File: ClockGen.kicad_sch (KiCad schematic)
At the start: 26 parts, among them Q1 2N4258, Q2 2N4258, Y1 XT0001

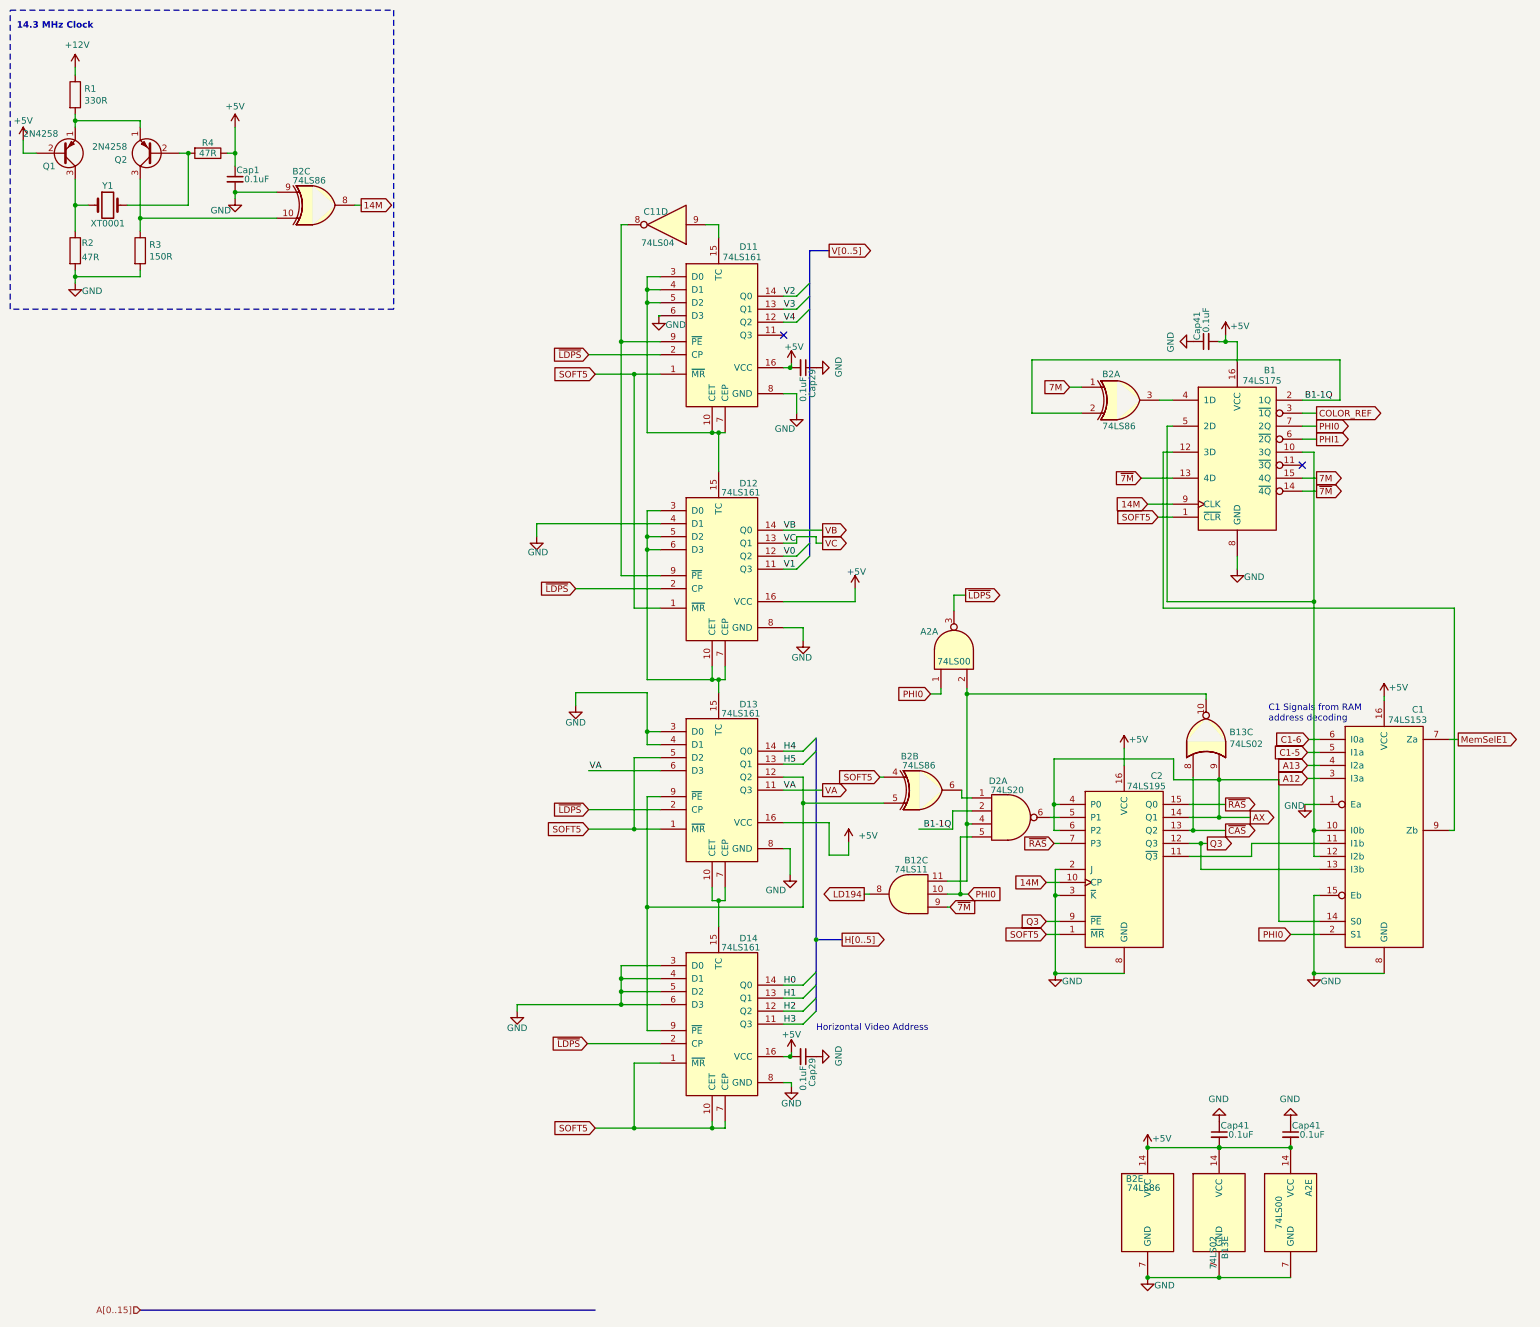
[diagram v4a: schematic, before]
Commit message: beautify capacitor footprint
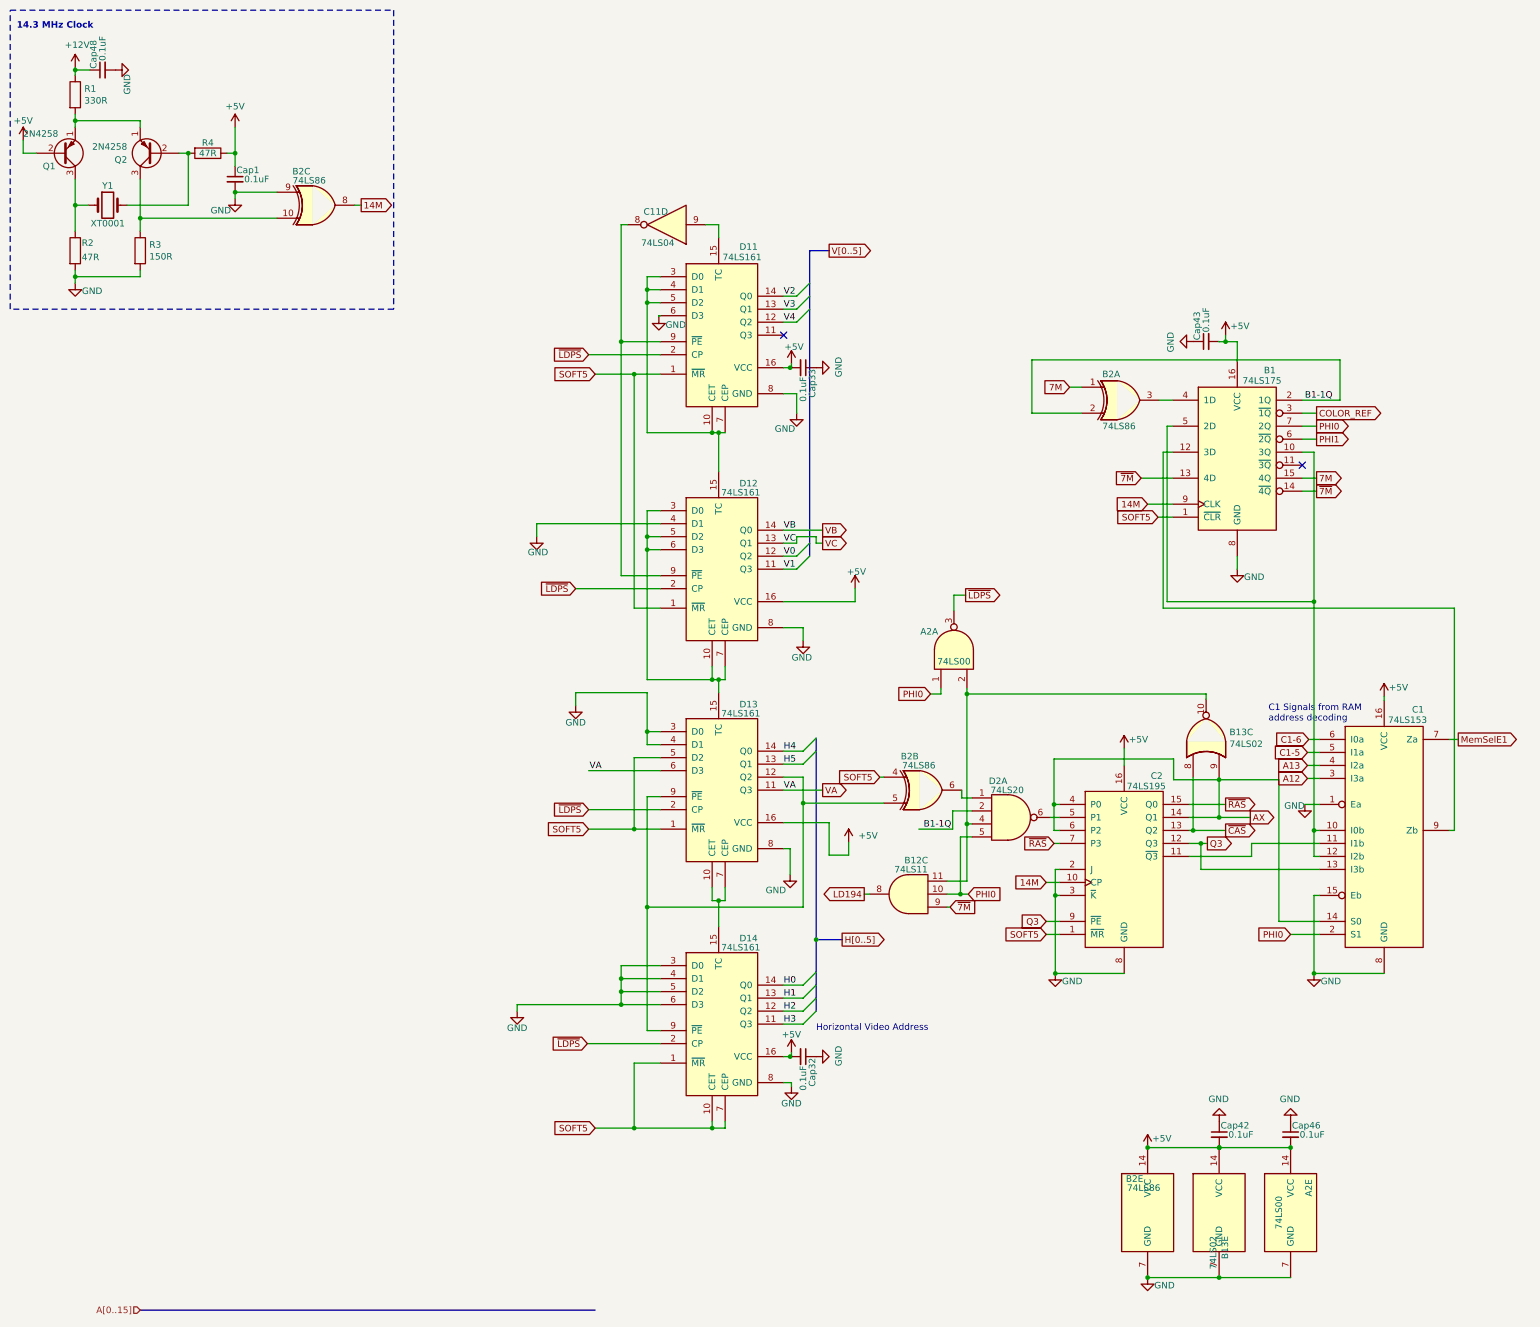
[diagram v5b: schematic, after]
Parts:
- added Cap48: 0.1uF, Capacitor_THT:C_Disc_D5.0mm_W2.5mm_P5.00mm, symbol Device:C_Small
- Cap46: renamed from Cap41; footprint Capacitor_THT:C_Disc_D5.0mm_W2.5mm_P5.00mm -> Apple-II:C_Disc_D5.0mm_W2.5mm_P5.00mm
- renumbered Cap29 to Cap32, Cap29 to Cap33, Cap41 to Cap42, Cap41 to Cap43
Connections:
- net +12V: now also Cap48.1
- net GND: now also Cap48.2
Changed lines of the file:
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@@
     (comment 2 "Modified by reifsnyderb to Rev. 0 and compared w/Rev. 0 gerbers my M. Willegal.")
+  )
+  (junction (at 25.4 24.384) (diameter 0) (color 0 0 0 0)
   )
   (junction (at 199.644 171.704) (diameter 0) (color 0 0 0 0)
@@
     (stroke (width 0) (type default))
   )
-  (wire (pts (xy 25.4 23.876) (xy 25.4 25.4))
+  (wire (pts (xy 25.4 23.876) (xy 25.4 24.384))
     (stroke (width 0) (type default))
   )
@@
     (stroke (width 0) (type default))
   )
+  (wire (pts (xy 25.4 24.384) (xy 28.194 24.384))
+    (stroke (width 0) (type default))
+  )
   (wire (pts (xy 243.078 172.974) (xy 243.84 172.974))
     (stroke (width 0) (type default))
@@
   )
   (wire (pts (xy 163.83 114.3) (xy 171.45 114.3))
+    (stroke (width 0) (type default))
+  )
+  (wire (pts (xy 25.4 24.384) (xy 25.4 25.4))
     (stroke (width 0) (type default))
   )
@@
   (symbol (lib_id "Device:C_Small") (at 246.38 77.4307 90) (unit 1)
     (in_bom yes) (on_board yes) (dnp no)
-    (property "Reference" "Cap41" (at 244.602 77.1767 0)
+    (property "Reference" "Cap43" (at 244.602 77.1767 0)
       (effects (font (size 1.27 1.27)) (justify left))
     )
@@
     (instances
       (project "AppleII"
-        (path "/f1f08369-4db3-46f7-9b89-a5d3cfbed55a/00000000-0000-0000-0000-000060210f9e"
-          (reference "Cap41") (unit 1)
-        )
         (path "/f1f08369-4db3-46f7-9b89-a5d3cfbed55a/00000000-0000-0000-0000-00006016cde0"
           (reference "Cap43") (unit 1)
@@
   (symbol (lib_id "Device:C_Small") (at 262.89 232.41 0) (unit 1)
     (in_bom yes) (on_board yes) (dnp no)
-    (property "Reference" "Cap41" (at 263.144 230.632 0)
+    (property "Reference" "Cap46" (at 263.144 230.632 0)
       (effects (font (size 1.27 1.27)) (justify left))
     )
@@
       (effects (font (size 1.27 1.27)) (justify left))
     )
-    (property "Footprint" "Capacitor_THT:C_Disc_D5.0mm_W2.5mm_P5.00mm" (at 262.89 232.41 0)
+    (property "Footprint" "Apple-II:C_Disc_D5.0mm_W2.5mm_P5.00mm" (at 262.89 232.41 0)
       (effects (font (size 1.27 1.27)) hide)
     )
@@
     (instances
       (project "AppleII"
-        (path "/f1f08369-4db3-46f7-9b89-a5d3cfbed55a/00000000-0000-0000-0000-000060210f9e"
-          (reference "Cap41") (unit 1)
-        )
         (path "/f1f08369-4db3-46f7-9b89-a5d3cfbed55a/00000000-0000-0000-0000-00006016cde0"
           (reference "Cap46") (unit 1)
@@
   (symbol (lib_id "Device:C_Small") (at 167.64 82.55 270) (unit 1)
     (in_bom yes) (on_board yes) (dnp no)
-    (property "Reference" "Cap29" (at 169.418 82.804 0)
+    (property "Reference" "Cap33" (at 169.418 82.804 0)
       (effects (font (size 1.27 1.27)) (justify left))
     )
@@
     (instances
       (project "AppleII"
-        (path "/f1f08369-4db3-46f7-9b89-a5d3cfbed55a/00000000-0000-0000-0000-00006039aab4"
-          (reference "Cap29") (unit 1)
-        )
         (path "/f1f08369-4db3-46f7-9b89-a5d3cfbed55a/00000000-0000-0000-0000-00006016cde0"
           (reference "Cap33") (unit 1)
@@
         (path "/f1f08369-4db3-46f7-9b89-a5d3cfbed55a/00000000-0000-0000-0000-00006016cde0"
           (reference "Q2") (unit 1)
+        )
+      )
+    )
+  )
+  (symbol (lib_id "power:GND") (at 33.274 24.384 90) (unit 1)
+    (in_bom yes) (on_board yes) (dnp no)
+    (property "Reference" "#PWR054" (at 39.624 24.384 0)
+      (effects (font (size 1.27 1.27)) hide)
+    )
+    (property "Value" "GND" (at 35.56 27.178 0)
+      (effects (font (size 1.27 1.27)))
+    )
+    (property "Footprint" "" (at 33.274 24.384 0)
+      (effects (font (size 1.27 1.27)) hide)
+    )
+    (property "Datasheet" "" (at 33.274 24.384 0)
+      (effects (font (size 1.27 1.27)) hide)
+    )
+    (pin "1")
+    (instances
+      (project "AppleII"
+        (path "/f1f08369-4db3-46f7-9b89-a5d3cfbed55a/00000000-0000-0000-0000-00006016cde0"
+          (reference "#PWR054") (unit 1)
         )
       )
@@
     )
   )
+  (symbol (lib_id "Device:C_Small") (at 30.734 24.384 90) (unit 1)
+    (in_bom yes) (on_board yes) (dnp no)
+    (property "Reference" "Cap48" (at 28.956 24.13 0)
+      (effects (font (size 1.27 1.27)) (justify left))
+    )
+    (property "Value" "0.1uF" (at 30.734 22.606 0)
+      (effects (font (size 1.27 1.27)) (justify left))
+    )
+    (property "Footprint" "Capacitor_THT:C_Disc_D5.0mm_W2.5mm_P5.00mm" (at 30.734 24.384 0)
+      (effects (font (size 1.27 1.27)) hide)
+    )
+    (property "Datasheet" "~" (at 30.734 24.384 0)
+      (effects (font (size 1.27 1.27)) hide)
+    )
+    (pin "1")
+    (pin "2")
+    (instances
+      (project "AppleII"
+        (path "/f1f08369-4db3-46f7-9b89-a5d3cfbed55a/00000000-0000-0000-0000-00006016cde0"
+          (reference "Cap48") (unit 1)
+        )
+      )
+    )
+  )
   (symbol (lib_id "74xx:74LS86") (at 234.95 247.65 0) (unit 5)
     (in_bom yes) (on_board yes) (dnp no)
@@
   (symbol (lib_id "power:GND") (at 170.18 217.17 90) (unit 1)
     (in_bom yes) (on_board yes) (dnp no)
-    (property "Reference" "#PWR028" (at 176.53 217.17 0)
+    (property "Reference" "#PWR031" (at 176.53 217.17 0)
       (effects (font (size 1.27 1.27)) hide)
     )
@@
     (instances
       (project "AppleII"
-        (path "/f1f08369-4db3-46f7-9b89-a5d3cfbed55a/00000000-0000-0000-0000-00006039aab4"
-          (reference "#PWR028") (unit 1)
-        )
         (path "/f1f08369-4db3-46f7-9b89-a5d3cfbed55a/00000000-0000-0000-0000-00006016cde0"
           (reference "#PWR031") (unit 1)
@@
   (symbol (lib_id "Device:C_Small") (at 167.64 217.17 270) (unit 1)
     (in_bom yes) (on_board yes) (dnp no)
-    (property "Reference" "Cap29" (at 169.418 217.424 0)
+    (property "Reference" "Cap32" (at 169.418 217.424 0)
       (effects (font (size 1.27 1.27)) (justify left))
     )
@@
     (instances
       (project "AppleII"
-        (path "/f1f08369-4db3-46f7-9b89-a5d3cfbed55a/00000000-0000-0000-0000-00006039aab4"
-          (reference "Cap29") (unit 1)
-        )
         (path "/f1f08369-4db3-46f7-9b89-a5d3cfbed55a/00000000-0000-0000-0000-00006016cde0"
           (reference "Cap32") (unit 1)
@@
   (symbol (lib_id "power:GND") (at 243.84 77.4307 270) (unit 1)
     (in_bom yes) (on_board yes) (dnp no)
-    (property "Reference" "#PWR041" (at 237.49 77.4307 0)
+    (property "Reference" "#PWR047" (at 237.49 77.4307 0)
       (effects (font (size 1.27 1.27)) hide)
     )
@@
     (instances
       (project "AppleII"
-        (path "/f1f08369-4db3-46f7-9b89-a5d3cfbed55a/00000000-0000-0000-0000-000060210f9e"
-          (reference "#PWR041") (unit 1)
-        )
         (path "/f1f08369-4db3-46f7-9b89-a5d3cfbed55a/00000000-0000-0000-0000-00006016cde0"
           (reference "#PWR047") (unit 1)
@@
   (symbol (lib_id "Device:C_Small") (at 248.9593 232.41 0) (unit 1)
     (in_bom yes) (on_board yes) (dnp no)
-    (property "Reference" "Cap41" (at 249.2133 230.632 0)
+    (property "Reference" "Cap42" (at 249.2133 230.632 0)
       (effects (font (size 1.27 1.27)) (justify left))
     )
@@
     (instances
       (project "AppleII"
-        (path "/f1f08369-4db3-46f7-9b89-a5d3cfbed55a/00000000-0000-0000-0000-000060210f9e"
-          (reference "Cap41") (unit 1)
-        )
         (path "/f1f08369-4db3-46f7-9b89-a5d3cfbed55a/00000000-0000-0000-0000-00006016cde0"
           (reference "Cap42") (unit 1)
@@
   (symbol (lib_id "power:GND") (at 262.89 229.87 180) (unit 1)
     (in_bom yes) (on_board yes) (dnp no)
-    (property "Reference" "#PWR041" (at 262.89 223.52 0)
+    (property "Reference" "#PWR050" (at 262.89 223.52 0)
       (effects (font (size 1.27 1.27)) hide)
     )
@@
     (instances
       (project "AppleII"
-        (path "/f1f08369-4db3-46f7-9b89-a5d3cfbed55a/00000000-0000-0000-0000-000060210f9e"
-          (reference "#PWR041") (unit 1)
-        )
         (path "/f1f08369-4db3-46f7-9b89-a5d3cfbed55a/00000000-0000-0000-0000-00006016cde0"
           (reference "#PWR050") (unit 1)
@@
   (symbol (lib_id "power:GND") (at 248.9593 229.87 180) (unit 1)
     (in_bom yes) (on_board yes) (dnp no)
-    (property "Reference" "#PWR041" (at 248.9593 223.52 0)
+    (property "Reference" "#PWR046" (at 248.9593 223.52 0)
       (effects (font (size 1.27 1.27)) hide)
     )
@@
     (instances
       (project "AppleII"
-        (path "/f1f08369-4db3-46f7-9b89-a5d3cfbed55a/00000000-0000-0000-0000-000060210f9e"
-          (reference "#PWR041") (unit 1)
-        )
         (path "/f1f08369-4db3-46f7-9b89-a5d3cfbed55a/00000000-0000-0000-0000-00006016cde0"
           (reference "#PWR046") (unit 1)
@@
   (symbol (lib_id "power:GND") (at 170.18 82.55 90) (unit 1)
     (in_bom yes) (on_board yes) (dnp no)
-    (property "Reference" "#PWR028" (at 176.53 82.55 0)
+    (property "Reference" "#PWR032" (at 176.53 82.55 0)
       (effects (font (size 1.27 1.27)) hide)
     )
@@
     (instances
       (project "AppleII"
-        (path "/f1f08369-4db3-46f7-9b89-a5d3cfbed55a/00000000-0000-0000-0000-00006039aab4"
-          (reference "#PWR028") (unit 1)
-        )
         (path "/f1f08369-4db3-46f7-9b89-a5d3cfbed55a/00000000-0000-0000-0000-00006016cde0"
           (reference "#PWR032") (unit 1)

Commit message: beautify resistors
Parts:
- Cap1, Cap32, Cap33, Cap42, Cap43, Cap48: footprint Capacitor_THT:C_Disc_D5.0mm_W2.5mm_P5.00mm -> Apple-II:C_Disc_D5.0mm_W2.5mm_P5.00mm
- R1, R2, R3, R4: footprint Resistor_THT:R_Axial_DIN0207_L6.3mm_D2.5mm_P10.16mm_Horizontal -> Apple-II:R_Axial_DIN0207_L6.3mm_D2.5mm_P10.16mm_Horizontal
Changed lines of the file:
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@@
       (effects (font (size 1.27 1.27)) (justify left))
     )
-    (property "Footprint" "Resistor_THT:R_Axial_DIN0207_L6.3mm_D2.5mm_P10.16mm_Horizontal" (at 23.622 29.21 90)
+    (property "Footprint" "Apple-II:R_Axial_DIN0207_L6.3mm_D2.5mm_P10.16mm_Horizontal" (at 23.622 29.21 90)
       (effects (font (size 1.27 1.27)) hide)
     )
@@
       (effects (font (size 1.27 1.27)) (justify left))
     )
-    (property "Footprint" "Resistor_THT:R_Axial_DIN0207_L6.3mm_D2.5mm_P10.16mm_Horizontal" (at 23.622 59.69 90)
+    (property "Footprint" "Apple-II:R_Axial_DIN0207_L6.3mm_D2.5mm_P10.16mm_Horizontal" (at 23.622 59.69 90)
       (effects (font (size 1.27 1.27)) hide)
     )
@@
       (effects (font (size 1.27 1.27)) (justify left))
     )
-    (property "Footprint" "Resistor_THT:R_Axial_DIN0207_L6.3mm_D2.5mm_P10.16mm_Horizontal" (at 36.322 59.69 90)
+    (property "Footprint" "Apple-II:R_Axial_DIN0207_L6.3mm_D2.5mm_P10.16mm_Horizontal" (at 36.322 59.69 90)
       (effects (font (size 1.27 1.27)) hide)
     )
@@
       (effects (font (size 1.27 1.27)))
     )
-    (property "Footprint" "Resistor_THT:R_Axial_DIN0207_L6.3mm_D2.5mm_P10.16mm_Horizontal" (at 51.308 38.862 90)
+    (property "Footprint" "Apple-II:R_Axial_DIN0207_L6.3mm_D2.5mm_P10.16mm_Horizontal" (at 51.308 38.862 90)
       (effects (font (size 1.27 1.27)) hide)
     )
@@
       (effects (font (size 1.27 1.27)) (justify left))
     )
-    (property "Footprint" "Capacitor_THT:C_Disc_D5.0mm_W2.5mm_P5.00mm" (at 56.642 45.72 0)
+    (property "Footprint" "Apple-II:C_Disc_D5.0mm_W2.5mm_P5.00mm" (at 56.642 45.72 0)
       (effects (font (size 1.27 1.27)) hide)
     )
@@
       (effects (font (size 1.27 1.27)) (justify left))
     )
-    (property "Footprint" "Capacitor_THT:C_Disc_D5.0mm_W2.5mm_P5.00mm" (at 246.38 77.4307 0)
+    (property "Footprint" "Apple-II:C_Disc_D5.0mm_W2.5mm_P5.00mm" (at 246.38 77.4307 0)
       (effects (font (size 1.27 1.27)) hide)
     )
@@
       (effects (font (size 1.27 1.27)) (justify left))
     )
-    (property "Footprint" "Capacitor_THT:C_Disc_D5.0mm_W2.5mm_P5.00mm" (at 167.64 82.55 0)
+    (property "Footprint" "Apple-II:C_Disc_D5.0mm_W2.5mm_P5.00mm" (at 167.64 82.55 0)
       (effects (font (size 1.27 1.27)) hide)
     )
@@
       (effects (font (size 1.27 1.27)) (justify left))
     )
-    (property "Footprint" "Capacitor_THT:C_Disc_D5.0mm_W2.5mm_P5.00mm" (at 30.734 24.384 0)
+    (property "Footprint" "Apple-II:C_Disc_D5.0mm_W2.5mm_P5.00mm" (at 30.734 24.384 0)
       (effects (font (size 1.27 1.27)) hide)
     )
@@
       (effects (font (size 1.27 1.27)) (justify left))
     )
-    (property "Footprint" "Capacitor_THT:C_Disc_D5.0mm_W2.5mm_P5.00mm" (at 167.64 217.17 0)
+    (property "Footprint" "Apple-II:C_Disc_D5.0mm_W2.5mm_P5.00mm" (at 167.64 217.17 0)
       (effects (font (size 1.27 1.27)) hide)
     )
@@
       (effects (font (size 1.27 1.27)) (justify left))
     )
-    (property "Footprint" "Capacitor_THT:C_Disc_D5.0mm_W2.5mm_P5.00mm" (at 248.9593 232.41 0)
-      (effects (font (size 1.27 1.27)) hide)
-    )
+    (property "Footprint" "Apple-II:C_Disc_D5.0mm_W2.5mm_P5.00mm" (at 248.9593 232.41 0)
+      (effects (font (size 1.27 1.27)) hide)
+    )
